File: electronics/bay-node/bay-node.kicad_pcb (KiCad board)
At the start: 4 copper layers, 74 x 90 mm, 105 parts, among them J1 ROW IN, J2 ROW OUT, J3 PC, J5 AUX, J6 CAM, J7 DATA, Q1 SUD50P06-15(UMW), Q2 2N7002, Q3 2N7002, Q4 AO3400A, SW1 RESET, SW2 BOOT, SW3 SERVICE, U1 LMR51635YDDCR, U10 INA226AIDGSR, U11 TJA1462AT, U12 USBLC6-2SC6, U13 USBLC6-2SC6, U2 AMS1117-3.3, U3 ESP32-S3-WROOM-1-N8R8, U4 USBLC6-2SC6, U5 MUX_PC, U6 MUX_DUT, U7 SN74LVC1G32DBVR, U8 USBLC6-2SC6, U9 TPS2553DDBVR

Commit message: Power pads connect solid: thermal reliefs only against tombstoning
A board declares its power nets (power_nets in design.py: GND, the bus,
the supplies, about 0.5 A and up).  pcbgen's power_pads() connects
their IC, connector and inductor pins, and any pad of 2.5 mm2 or more,
solid to the pours: one 0.4 mm spoke was the narrowest point of the
current's path.  A small part gets the same connection on every end
(solid where every end sits on a pour, reliefs where one is a track);
through-hole pins keep reliefs (0.8 mm spokes if hand-soldered).  The
.kicad_dru says it too: the power pins connect solid, and a power net's
relieved pads keep its minimum spokes.

Hub: J1's GND, the row connectors' GND, the eFuses' GND pins and pads,
the buck, the LDO, C8, D1 solid; C1, C2, C11-C14 solid on both ends.
Node: U9's input island solid, J7's and the camera's GND, the ICs'
GND, C1, D2; C12 and C20 solid on both ends.  Same routes re-imported:
ERC/DRC 0, parity 0; the CPL is unchanged.  Fabio's rule reworded in
review-konnect.md.

Co-Authored-By: Claude Opus 5.5 <noreply@anthropic.com>
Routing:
- net GND: track 73.0 -> 69.3 mm, vias 240 -> 244

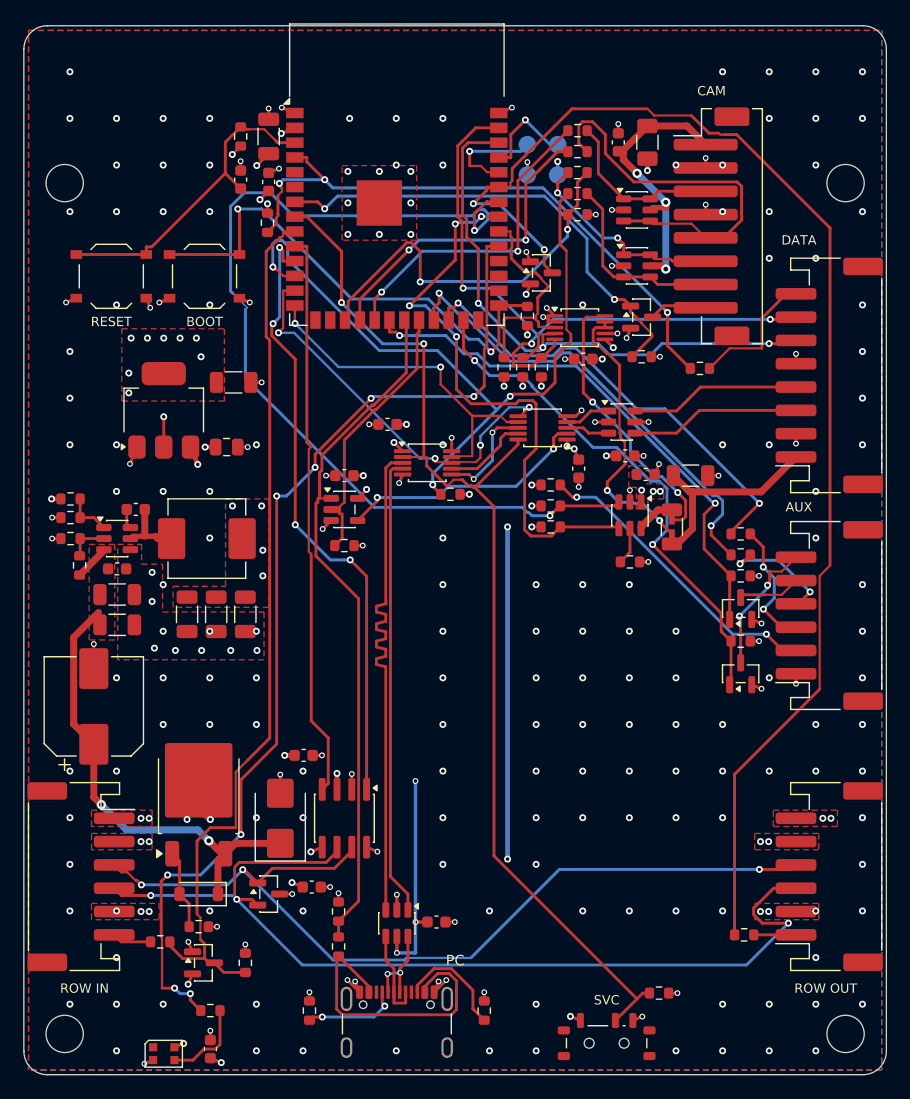
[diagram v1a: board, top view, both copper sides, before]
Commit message: Boards: tracks straightened after routing, bends ranked; bay node and hub re-routed
Freerouting leaves staircases of 45° and straight segments where one bend
would do: they are no longer than the straight route, so nothing preferred it.

- pcbgen.tidy_tracks now runs on every board after the import: a run of up
  to 12 router segments becomes the fewest straight and 45° segments joining
  its ends (octilinear.py: one, one bend, or a dogleg on one of the run's own
  lines), at no more length and with every clearance kept.  Differential
  pairs, drawn tracks, exclusive cores, fan-out reservations and footprint
  keep-outs are left alone.  tools/kicad.sh <board> --tidy runs it on a
  routed board without re-routing.
- route_metrics counts bends; route_farm ranks them at 0.5 mm each.
- Bay node: In2's +5V outline stops at x 21.7, off the +3V3 one.  Re-routed
  by the portfolio (noneck): 504 bends, 435 vias, 2183 mm (was 631, 401, 2270).
- Power hub: buck-vin is exclusive (14 of 17 runs clean, 2 before).
  Re-routed (planevia50): 655 bends, 436 vias, 3447 mm (was 767, 433, 3537).
- DATA x4 v2: the drawn switch feeds stay (no clean run without them); its
  routing straightened in place, the tidy settings now the default.
- Camera pod straightened in place (59 -> 48 bends); data port unchanged.

ERC, copper DRC and parity clean on all five; fab outputs, the DATA x4 v2
panel and the viewer's models regenerated.

Co-Authored-By: Claude Opus 5.5 <noreply@anthropic.com>
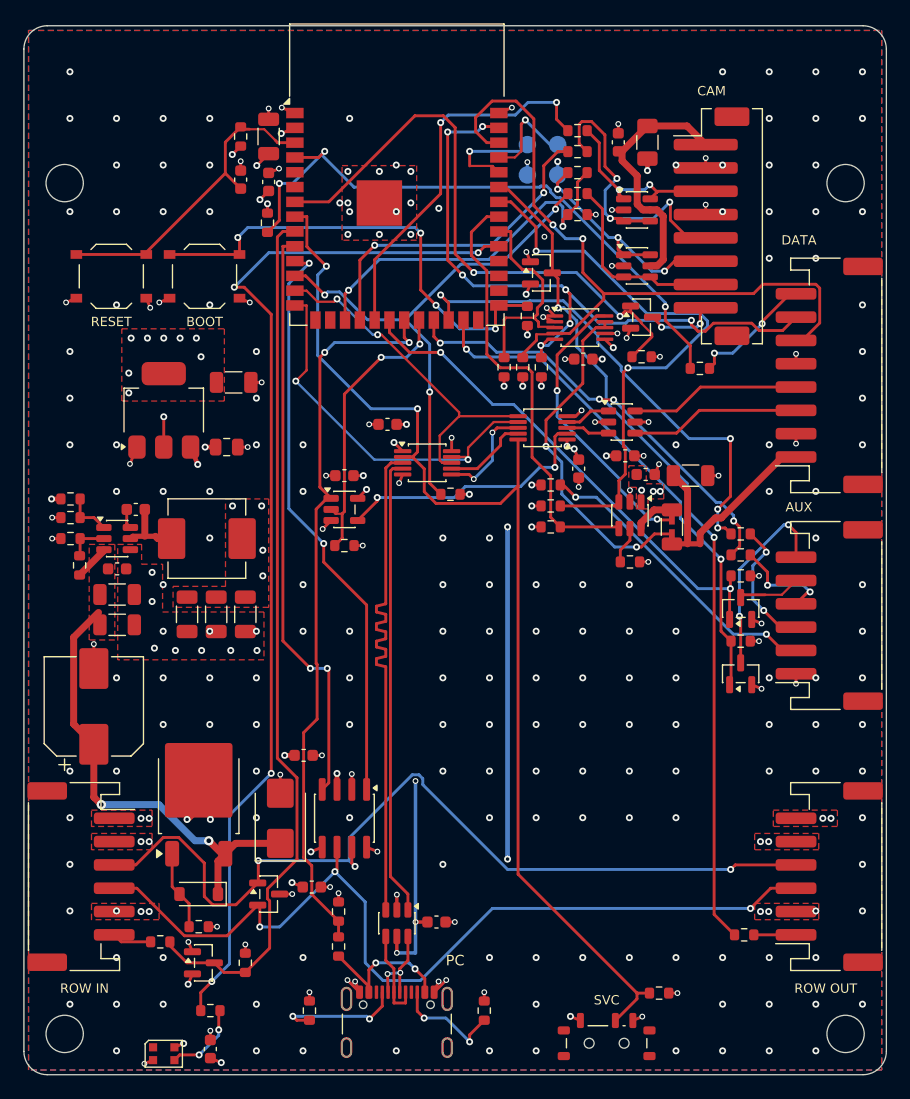
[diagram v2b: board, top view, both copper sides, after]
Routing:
- net POS_OUT: track 113.3 -> 73.2 mm
- net DUT_EN: track 82.6 -> 49.2 mm
- net CAM_CS: track 63.5 -> 46.1 mm
- net /USB/PC_VBUS: track 25.8 -> 12.6 mm, vias 0 -> 2
- net DUT_FLT_N: track 49.8 -> 37.8 mm, vias 4 -> 0
- net CAM_LED: track 40.9 -> 51.3 mm
- net I2C_SDA: track 52.7 -> 62.8 mm, vias 3 -> 2
- net CAN_L: track 84.8 -> 77.4 mm
- net /Camera/CAM_MOSI_C: track 34.1 -> 28.0 mm, vias 0 -> 3
- net ESP_DN: track 35.4 -> 29.6 mm, vias 4 -> 2
- net /DUT power & AUX/AUX_BOOT_N: track 11.7 -> 16.9 mm
- net /DUT power & AUX/SHUNT_N: track 24.5 -> 29.7 mm
- net CAM_SCK: track 27.9 -> 32.8 mm
- net /Camera/CAM_MISO_C: track 17.8 -> 21.7 mm, vias 2 -> 3
- net CAN_TXD: track 53.5 -> 49.9 mm, vias 4 -> 2
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
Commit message: Node 5 V buck: LMR51625 with TI's 4.7 µH
The bay node's U1 goes from the LMR51635YDDCR (3.5 A) to its 2.5 A
sibling, the LMR51625YDDCR (C44991044), as the user asked.  TI SLUSF64B
covers both parts: they have the same DDC package and pinout (FB 1,
EN 2, VIN 3, GND 4, SW 5, CB 6), the same 0.8 V reference, the same EN
thresholds and the same 63 V absolute maximum.

L1 goes to 4.7 µH, per SLUSF64B table 8-1 (LMR51625, 5 V, 1.1 MHz).
The new part is the FXL0630-4R7-M (C167220), in the same footprint:
9 A saturation, 6 A rms, 33 mΩ.  The existing 3 × 22 µF output meets
the table's 22 µF.

Current headroom: a bay draws at most 2.2 A (node 0.30 A, the DUT
switch's 1.52 A, camera 0.36 A).  From 28 V the inductor then peaks at
about 2.6 A (0.8 A ripple), under the 2.5 A part's 2.9 A minimum peak
limit.  With 3.3 µH the peak would be 2.74 A.

The hub keeps the LMR51635 under the "buck" catalogue key.  The node
uses two new keys, "buck25" and "buck_l47".

CPL: JLC's EasyEDA footprint of C44991044 is pad for pad that of
C45262770 and C7519, so it gets the same 270° correction.  C167220
shares C167219's footprint and needs no correction.

Board: schematic regenerated; the routed PCB keeps its routing (only
U1 and L1 properties change, copied from a fresh build).  ERC 0,
DRC 0, unconnected 0, parity 0.  Gerbers, CPL and renders unchanged.

Cost:
- node order $322.96 -> $316.95 (-$6.01 components: LCSC $1.0744
  against $1.5997 at 10, the inductor $0.096 against $0.107, × 1.12);
- one rack's JLC boards $752.95 -> $746.43 (5 racks $310.59,
  10 racks $257.85);
- BOM total €1,013 -> €1,007 (€126 a bay);
- the 9-instead-of-10 lever is now $2.34.

The parts snapshot gains the two parts.  The BOM note prints a
negative adjustment as "− $6.01", not "+ $-6.01".

Co-Authored-By: Claude Opus 5.5 <noreply@anthropic.com>
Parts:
- L1: value 3.3u -> 4.7u
- U1: value LMR51635YDDCR -> LMR51625YDDCR
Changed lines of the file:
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@@
 			)
 		)
-		(property "Value" "3.3u"
+		(property "Value" "4.7u"
 			(at 0 4.25 0)
 			(layer "F.Fab")
@@
 			)
 		)
-		(property "Description" "3.3 µH, 9.5 A sat, 8.5 A rms, 22 mΩ, molded"
+		(property "Description" "4.7 µH, 9 A sat, 6 A rms, 33 mΩ, molded"
 			(at 0 0 0)
 			(layer "F.Fab")
@@
 			)
 		)
-		(property "MPN" "FXL0630-3R3-M"
+		(property "MPN" "FXL0630-4R7-M"
 			(at 0 0 0)
 			(layer "F.Fab")
@@
 			)
 		)
-		(property "LCSC" "C167219"
+		(property "LCSC" "C167220"
 			(at 0 0 0)
 			(layer "F.Fab")
@@
 			)
 		)
-		(property "Value" "LMR51635YDDCR"
+		(property "Value" "LMR51625YDDCR"
 			(at 0 2.4 0)
 			(layer "F.Fab")
@@
 			)
 		)
-		(property "Datasheet" "https://www.ti.com/lit/ds/symlink/lmr51635.pdf"
+		(property "Datasheet" "https://www.ti.com/lit/ds/symlink/lmr51625.pdf"
 			(at 0 0 0)
 			(layer "F.Fab")
@@
 			)
 		)
-		(property "Description" "4.3–60 V 3.5 A synchronous buck, 1.1 MHz, PFM + spread spectrum"
+		(property "Description" "4.3–60 V 2.5 A synchronous buck, 1.1 MHz, PFM + spread spectrum"
 			(at 0 0 0)
 			(layer "F.Fab")
@@
 			)
 		)
-		(property "MPN" "LMR51635YDDCR"
+		(property "MPN" "LMR51625YDDCR"
 			(at 0 0 0)
 			(layer "F.Fab")
@@
 			)
 		)
-		(property "LCSC" "C45262770"
+		(property "LCSC" "C44991044"
 			(at 0 0 0)
 			(layer "F.Fab")
@@
 			)
 		)
-		(property "Alternative" "LMR51635YFDDCR (C44750836): same, forced PWM, no spread spectrum"
+		(property "Alternative" "LMR51625YFDDCR (C45262768): same, forced PWM, no spread spectrum; LMR51635YDDCR (C45262770): 3.5 A, 3.3 µH"
 			(at 0 0 0)
 			(layer "F.Fab")

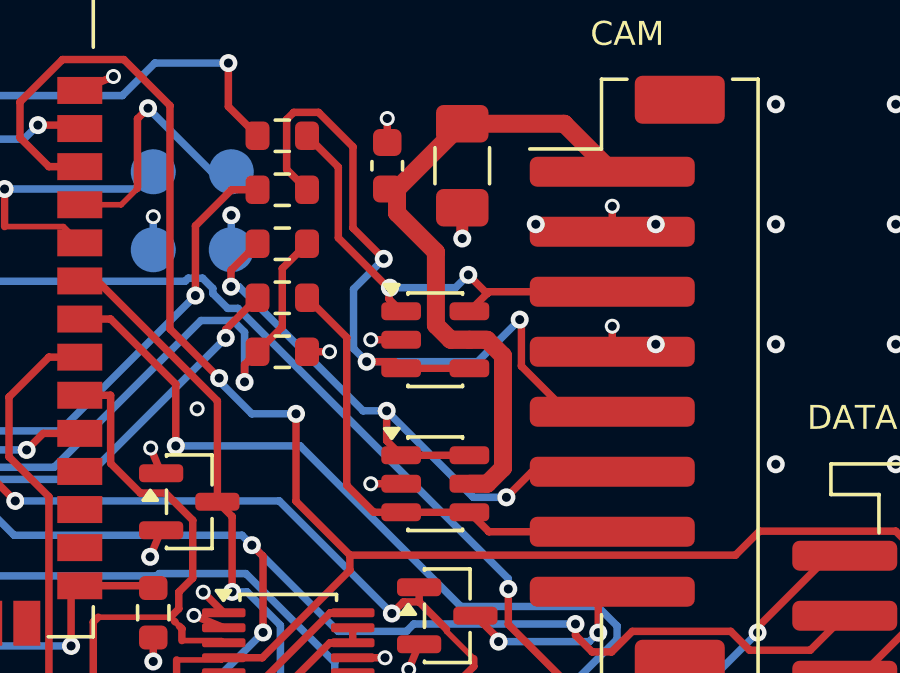
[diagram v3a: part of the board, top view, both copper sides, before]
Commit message: Bay node: AP2114H for the 3.3 V, camera ESD clamped to +3V3
The schematic counter-review's fixes, approved by the user.

- U2: AP2114H-3.3TRG1 (C150716, catalog ldo_1a) instead of the AMS1117-3.3.
  It is specified stable with ceramics (C11, C12); the AMS1117 guarantees it
  only with 22 uF tantalum.  Same SOT-223 "H" pinout (1 GND, 2 and tab VOUT,
  3 VIN), footprint and copper: only the part's properties change.
- U12, U13 (USBLC6 on the camera lead): pin 5 on +3V3 instead of CAM_5V.
  With CAM_5V off (the PTC tripped), the SPI lines would feed the pod through
  the upper diodes, and CAM_5V's clamp sits above the ESP32's 3.6 V.  A
  minimal patch of the routing, no re-route: the CAM_5V stub that only
  reached the two pins goes (10 segments); U12.5 gets a +3V3 feed to a via in
  In2's +3V3 area; U13.5, with no room for its own, joins U12.5 along the
  stub's old east path at 0.25 mm.  The straightening pass ran on +3V3 and
  CAM_5V.
- Stale notes: AUX_VREF goes through R23's 1k, not 33 ohms; the next node's
  pull-down is R29's 470k, not 100k.
- pcbgen.fanout_pads takes `only` (REF.PAD), to fan out a few pads of a
  routed board.

ERC 0, DRC 0, unconnected 0, parity 0, every 3D model found.  The renders,
Gerbers and viewer model are regenerated (the unchanged iso render kept).
The schematic, the BOM and the docs (the node table, the CPL fix table, the
bring-up check, PCBA review N9) follow.  The hub and bom/ are untouched.

Co-Authored-By: Claude Opus 5.5 <noreply@anthropic.com>
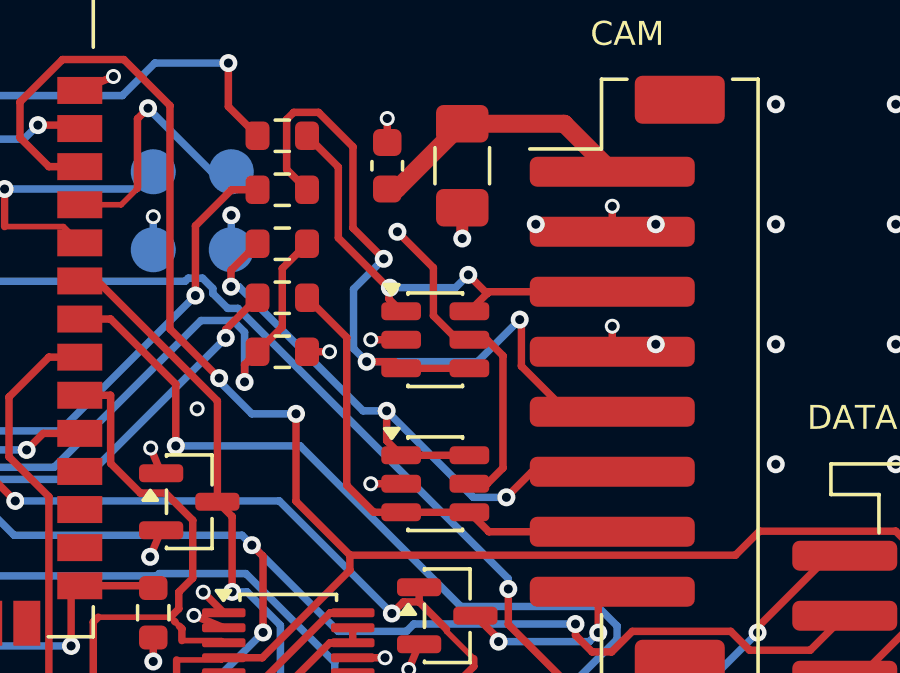
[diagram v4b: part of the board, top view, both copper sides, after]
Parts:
- U2: value AMS1117-3.3 -> AP2114H-3.3TRG1
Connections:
- U12 pad 5: /Camera/CAM_5V -> +3V3
- U13 pad 5: /Camera/CAM_5V -> +3V3
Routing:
- net /Camera/CAM_5V: track 21.9 -> 9.06 mm
- net +3V3: track 58.3 -> 69.5 mm, vias 40 -> 41
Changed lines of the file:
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@@
 			)
 		)
-		(property "Value" "AMS1117-3.3"
+		(property "Value" "AP2114H-3.3TRG1"
 			(at 0 4.5 90)
 			(layer "F.Fab")
@@
 			)
 		)
-		(property "Datasheet" ""
+		(property "Datasheet" "https://www.diodes.com/assets/Datasheets/AP2114.pdf"
 			(at 0 0 90)
 			(unlocked yes)
@@
 			)
 		)
-		(property "Description" "3.3 V 1 A LDO"
+		(property "Description" "3.3 V 1 A LDO, 450 mV dropout at 1 A, SOT-223"
 			(at 0 0 90)
 			(unlocked yes)
@@
 			)
 		)
-		(property "MPN" "AMS1117-3.3"
+		(property "MPN" "AP2114H-3.3TRG1"
 			(at 0 0 90)
 			(layer "F.Fab")
@@
 			)
 		)
-		(property "Manufacturer" "AMS"
+		(property "Manufacturer" "Diodes Incorporated"
 			(at 0 0 90)
 			(layer "F.Fab")
@@
 			)
 		)
-		(property "LCSC" "C6186"
+		(property "LCSC" "C150716"
 			(at 0 0 90)
 			(layer "F.Fab")
@@
 			(layers "F.Cu" "F.Mask" "F.Paste")
 			(roundrect_rratio 0.25)
-			(net "/Camera/CAM_5V")
+			(net "+3V3")
 		)
 		(pad "6" smd roundrect
@@
 			(layers "F.Cu" "F.Mask" "F.Paste")
 			(roundrect_rratio 0.25)
-			(net "/Camera/CAM_5V")
+			(net "+3V3")
 		)
 		(pad "6" smd roundrect
@@
 	)
 	(segment
+		(start 54.3323 20.6)
+		(end 54.857 20.0753)
+		(width 0.25)
+		(layer "F.Cu")
+		(net "+3V3")
+	)
+	(segment
 		(start 47.75 85.35)
 		(end 46.894572 84.99567)
@@
 	)
 	(segment
+		(start 52.5375 13.4)
+		(end 51.3375 12.2)
+		(width 0.25)
+		(locked yes)
+		(layer "F.Cu")
+		(net "+3V3")
+	)
+	(segment
 		(start 49.85 26.9)
 		(end 50.570342 27.620342)
@@
 	)
 	(segment
+		(start 54.857 16.3323)
+		(end 54.3247 15.8)
+		(width 0.25)
+		(layer "F.Cu")
+		(net "+3V3")
+	)
+	(segment
 		(start 44.4 30.125)
 		(end 44.4 30.925)
@@
 	)
 	(segment
+		(start 53.7375 15.8)
+		(end 53.3375 15.8)
+		(width 0.25)
+		(locked yes)
+		(layer "F.Cu")
+		(net "+3V3")
+	)
+	(segment
 		(start 21 14.175)
 		(end 20.254657 14.920342)
@@
 	)
 	(segment
+		(start 52.5375 15)
+		(end 52.5375 13.4)
+		(width 0.25)
+		(locked yes)
+		(layer "F.Cu")
+		(net "+3V3")
+	)
+	(segment
 		(start 43.4625 22.15)
 		(end 43.095356 23.036363)
@@
 	)
 	(segment
+		(start 53.7375 20.6)
+		(end 54.3323 20.6)
+		(width 0.25)
+		(layer "F.Cu")
+		(net "+3V3")
+	)
+	(segment
+		(start 54.857 20.0753)
+		(end 54.857 16.3323)
+		(width 0.25)
+		(layer "F.Cu")
+		(net "+3V3")
+	)
+	(segment
+		(start 54.3247 15.8)
+		(end 53.7375 15.8)
+		(width 0.25)
+		(layer "F.Cu")
+		(net "+3V3")
+	)
+	(segment
+		(start 53.3375 15.8)
+		(end 52.5375 15)
+		(width 0.25)
+		(locked yes)
+		(layer "F.Cu")
+		(net "+3V3")
+	)
+	(segment
 		(start 12 36.15)
 		(end 12 33.55)
@@
 	)
 	(via
+		(at 51.3375 12.2)
+		(size 0.6)
+		(drill 0.3)
+		(layers "F.Cu" "B.Cu")
+		(locked yes)
+		(net "+3V3")
+	)
+	(via
 		(at 41.5 43)
 		(size 0.6)
@@
 	)
 	(segment
-		(start 52.6207 15.3114)
-		(end 52.6207 12.8741)
-		(width 0.6)
-		(layer "F.Cu")
-		(net "/Camera/CAM_5V")
-	)
-	(segment
 		(start 56.9 8.6)
 		(end 53.5 8.6)
@@
 	)
 	(segment
-		(start 54.3247 15.8)
-		(end 53.7375 15.8)
-		(width 0.6)
-		(layer "F.Cu")
-		(net "/Camera/CAM_5V")
-	)
-	(segment
-		(start 51.325 11.5784)
-		(end 51.325 10.775)
-		(width 0.6)
-		(layer "F.Cu")
-		(net "/Camera/CAM_5V")
-	)
-	(segment
-		(start 54.857 20.0753)
-		(end 54.857 16.3323)
-		(width 0.6)
-		(layer "F.Cu")
-		(net "/Camera/CAM_5V")
-	)
-	(segment
 		(start 53.5 8.6)
 		(end 51.325 10.775)
@@
 	)
 	(segment
-		(start 52.6207 12.8741)
-		(end 51.325 11.5784)
-		(width 0.6)
-		(layer "F.Cu")
-		(net "/Camera/CAM_5V")
-	)
-	(segment
-		(start 53.7375 15.8)
-		(end 53.1093 15.8)
-		(width 0.6)
-		(layer "F.Cu")
-		(net "/Camera/CAM_5V")
-	)
-	(segment
 		(start 51.325 10.775)
 		(end 51 10.775)
 		(width 0.6)
 		(layer "F.Cu")
-		(net "/Camera/CAM_5V")
-	)
-	(segment
-		(start 54.3323 20.6)
-		(end 54.857 20.0753)
-		(width 0.6)
-		(layer "F.Cu")
-		(net "/Camera/CAM_5V")
-	)
-	(segment
-		(start 53.7375 20.6)
-		(end 54.3323 20.6)
-		(width 0.6)
-		(layer "F.Cu")
-		(net "/Camera/CAM_5V")
-	)
-	(segment
-		(start 53.1093 15.8)
-		(end 52.6207 15.3114)
-		(width 0.6)
-		(layer "F.Cu")
-		(net "/Camera/CAM_5V")
-	)
-	(segment
-		(start 54.857 16.3323)
-		(end 54.3247 15.8)
-		(width 0.6)
-		(layer "F.Cu")

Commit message: Schematic review S1, S4, S6: POS_IN 150k, the hub's ON LEDs on 18k, the camera's 0.75 A PTC
The user approved them ("S1 oui / S6 oui / S4 oui").

* S1, bay node: R29 470k -> 150k (C22807, basic).
  - Before its firmware runs, the upstream POS output (a node's IO42, the
    hub's IO10-13) floats. The BAT54S's warm leakage (about 2-3 uA at
    65 C) could then lift POS_IN through 470k to VIL.
  - Driven high through R30 + R28, 150k still gives 2.87 V, above VIH.
  - The design.py notes and bay_node.dtsi follow.
* S4, power hub: R41-R44 (the ON LEDs on the row outputs) 10k -> 18k
  (C25810, already on the board): 1.4 mA and 37 mW at 28 V. The 10k
  ran at 75 % of its 0603 rating at 29.4 V.
* S6, bay node: F1 (CAM_5V) goes from the 0.5 A PTC to SMD1206P075TF
  (RUILON, C20987, new catalog key pptc750): 0.75 A hold, 1.5 A trip,
  the same 1206 footprint. It is extended like C20799, so no fee changes.
  - Arducam gives the Mega 317 mA working: with the LEDs that is
    ~0.42 A on CAM_5V, where the 0.5 A part holds ~0.31 A at 70 C.
  - The camera pod's LDO tab gets the copper its routing leaves: a
    top-side +3V3 pour round the tab and a bottom-side island, joined by
    three vias. U1 drops ~0.5 W at 317 mA. The routing is unchanged.
  - The "~120 mA" notes go to 317 mA (node and pod design.py,
    electronics.md).
  - The bay's worst case follows: <= 2.25 A on +5V, the buck's inductor
    peaking at ~2.65 A (under its 2.9 A minimum limit), 13.5 W from
    VRACK (power-distribution-review.md, the buck notes).

The routed PCBs keep their routing.
- Node and hub: only the changed parts' properties (KiCad's Python, as
  pcbgen sets them).
- Pod: the two new zones and three vias, refilled.
- ERC 0, DRC 0, unconnected 0, parity 0 on all three (run on the Mac:
  zephyrbox didn't answer).
- keep_unchanged kept the node's renders and the hub's Gerbers. The
  hub's bottom render is restored: 9 pixels of via-hole noise, as before.
- The pod's renders, Gerbers and viewer GLB chang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
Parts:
- F1: value 0.5A -> 0.75A
- R29: value 470k -> 150k
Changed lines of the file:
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@@
 			)
 		)
-		(property "Value" "0.5A"
+		(property "Value" "0.75A"
 			(at 0 1.83 90)
 			(layer "F.Fab")
@@
 			)
 		)
-		(property "Description" "PTC 0.5 A hold, 1206"
+		(property "Description" "PTC 0.75 A hold, 1.5 A trip, 1206"
 			(at 0 0 90)
 			(layer "F.Fab")
@@
 			)
 		)
-		(property "MPN" "SMD1206P050TF"
+		(property "MPN" "SMD1206P075TF"
 			(at 0 0 90)
 			(layer "F.Fab")
@@
 			)
 		)
-		(property "LCSC" "C20799"
+		(property "LCSC" "C20987"
 			(at 0 0 90)
 			(layer "F.Fab")
@@
 			)
 		)
-		(property "Value" "470k"
+		(property "Value" "150k"
 			(at 0 1.43 90)
 			(layer "F.Fab")
@@
 			)
 		)
-		(property "Description" "Resistor 470k 0603"
+		(property "Description" "Resistor 150k 0603"
 			(at 0 0 90)
 			(layer "F.Fab")
@@
 			)
 		)
-		(property "LCSC" "C23178"
+		(property "LCSC" "C22807"
 			(at 0 0 90)
 			(layer "F.Fab")
@@
 			)
 		)
-		(property "MPN" "0603WAF4703T5E"
+		(property "MPN" "0603WAF1503T5E"
 			(at 0 0 90)
 			(layer "F.Fab")
